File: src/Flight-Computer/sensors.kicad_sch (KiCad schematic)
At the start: 6 parts, among them U8 MPU-9250

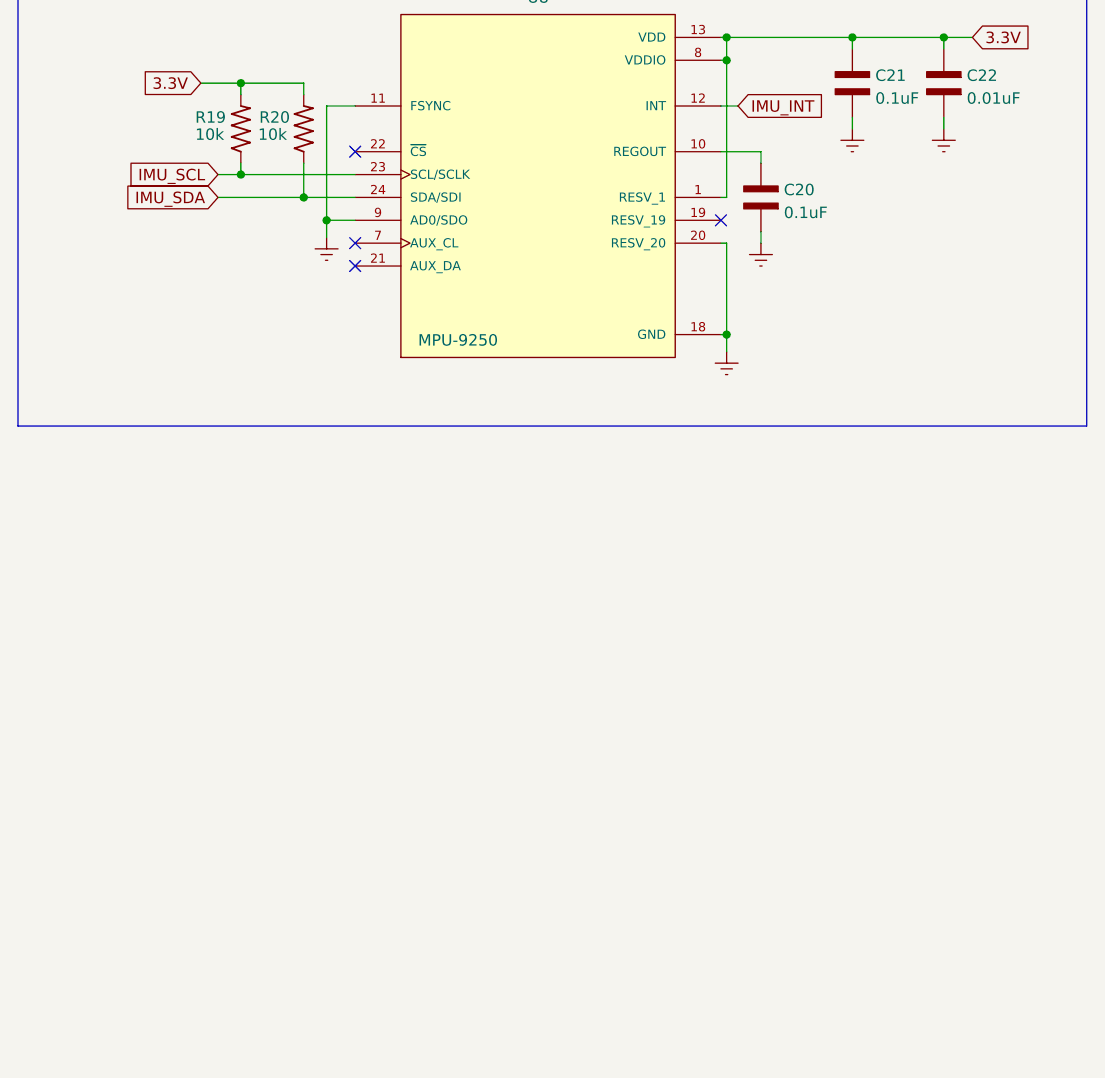
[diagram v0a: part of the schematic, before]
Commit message: added backup battery to lib files
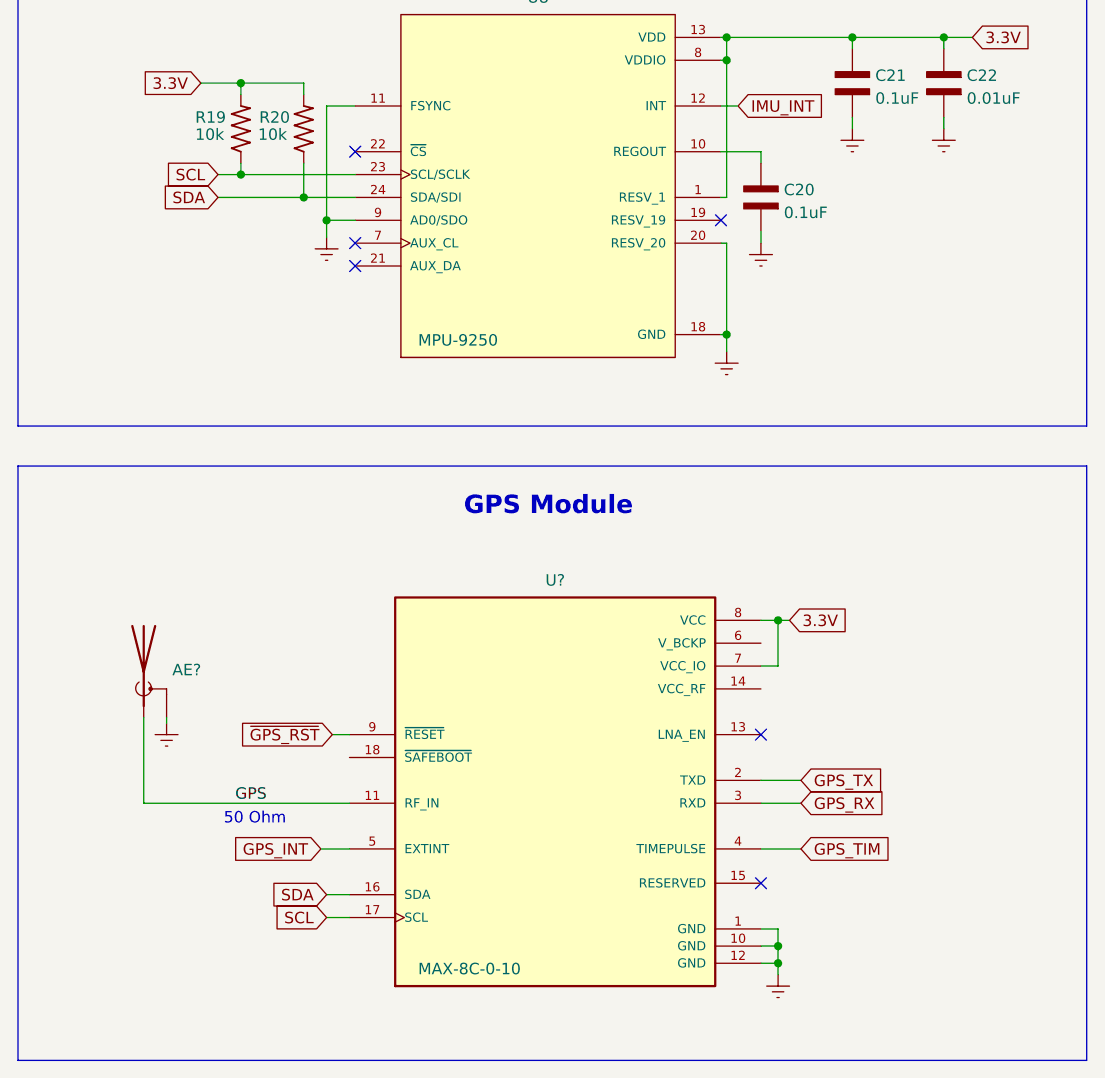
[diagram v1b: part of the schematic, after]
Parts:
- added AE?: 0734120110, symbol Flight-Computer:0734120110
- added U?: MAX-8C-0-10, XCVR_MAX-8C-0-10, symbol Flight-Computer:MAX-8C-0-10
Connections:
- net 3.3V: now also U?.7 (VCC_IO), U?.8 (VCC)
- net Earth: now also AE?.2 (Shield), U?.1 (GND), U?.10 (GND), U?.12 (GND)
- net IMU_SCL renamed SCL
- net SCL: now also U?.17 (SCL)
- net IMU_SDA renamed SDA
- net SDA: now also U?.16 (SDA)
- new net GPS: AE?.1 (A), U?.11 (RF_IN)
- new net GPS_INT: U?.5 (EXTINT)
- new net GPS_RX: U?.3 (RXD)
- new net GPS_TIM: U?.4 (TIMEPULSE)
- new net GPS_TX: U?.2 (TXD)
- new net ~{GPS_RST}: U?.9 (~{RESET})
- no-connect marks 4 -> 6
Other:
- note added: "50 Ohm"
- note added: "GPS Module"

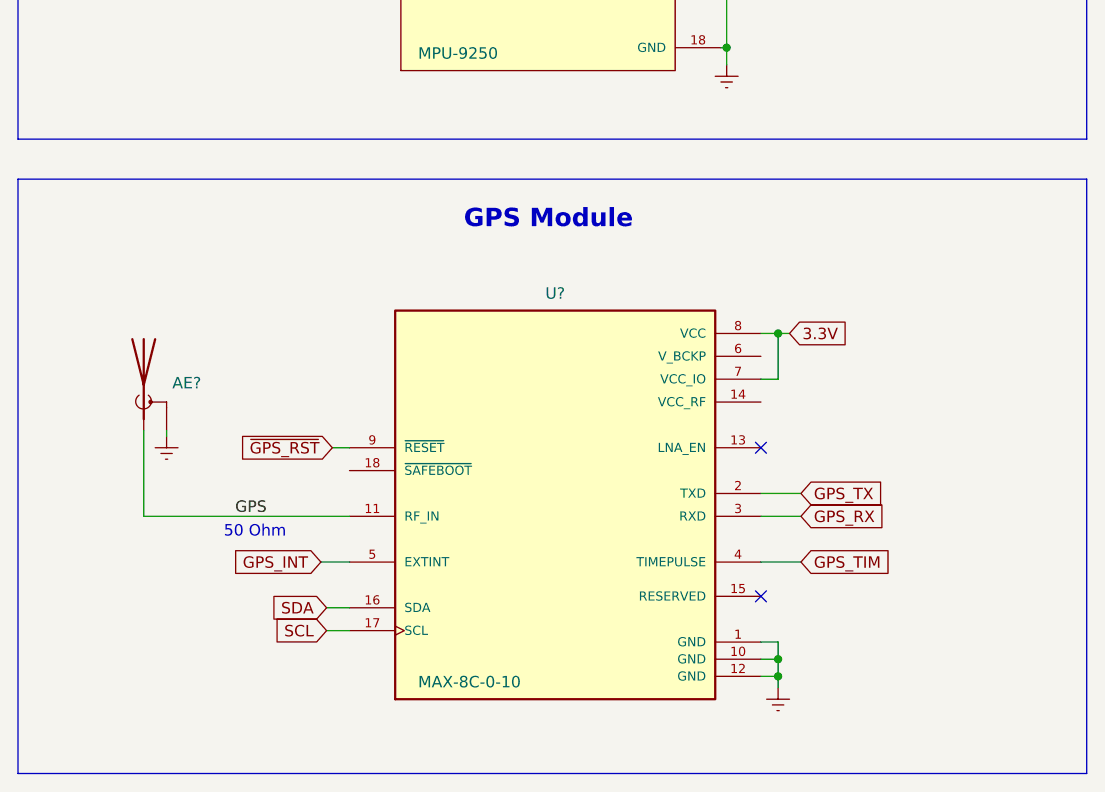
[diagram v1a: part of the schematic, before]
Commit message: implemented gps module for passive antenna design
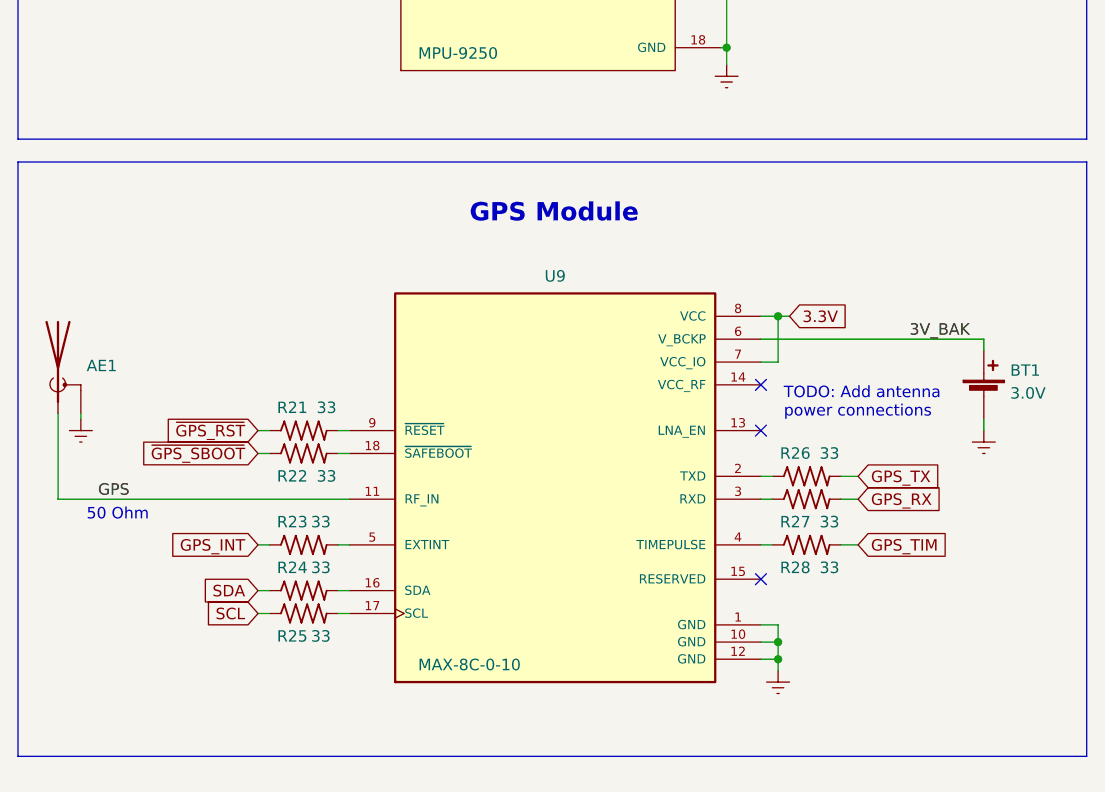
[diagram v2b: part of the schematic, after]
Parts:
- added BT1: MS614SE-FL28E, symbol Flight-Computer:MS614SE-FL28E
- added R21, R22, R23, R24, R25, R26, R27, R28: 33, symbol Flight-Computer:RES_0603
- gave numbers to parts that had none: 2
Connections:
- net Earth: now also BT1.2 (-)
- net GPS_INT: now also R23.1; no longer U9.5 (EXTINT)
- net GPS_RX: now also R27.2; no longer U9.3 (RXD)
- net GPS_TIM: now also R28.2; no longer U9.4 (TIMEPULSE)
- net GPS_TX: now also R26.2; no longer U9.2 (TXD)
- net SCL: now also R25.1; no longer U9.17 (SCL)
- net SDA: now also R24.1; no longer U9.16 (SDA)
- net ~{GPS_RST}: now also R21.1; no longer U9.9 (~{RESET})
- net at U9.18 (~{SAFEBOOT}): now also R22.2
- net 3V_BAK: now reaches U9.6 (V_BCKP)
- net 3V_BAK: now also BT1.1 (+)
- new net: R25.2, U9.17 (SCL)
- new net: R28.1, U9.4 (TIMEPULSE)
- new net: R23.2, U9.5 (EXTINT)
- new net: R24.2, U9.16 (SDA)
- new net: R26.1, U9.2 (TXD)
- new net: R27.1, U9.3 (RXD)
- new net: R21.2, U9.9 (~{RESET})
- new net ~{GPS_SBOOT}: R22.1
- no-connect marks 6 -> 7
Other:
- note added: "TODO: Add antenna power connections"
- moved on the sheet: AE1, U9

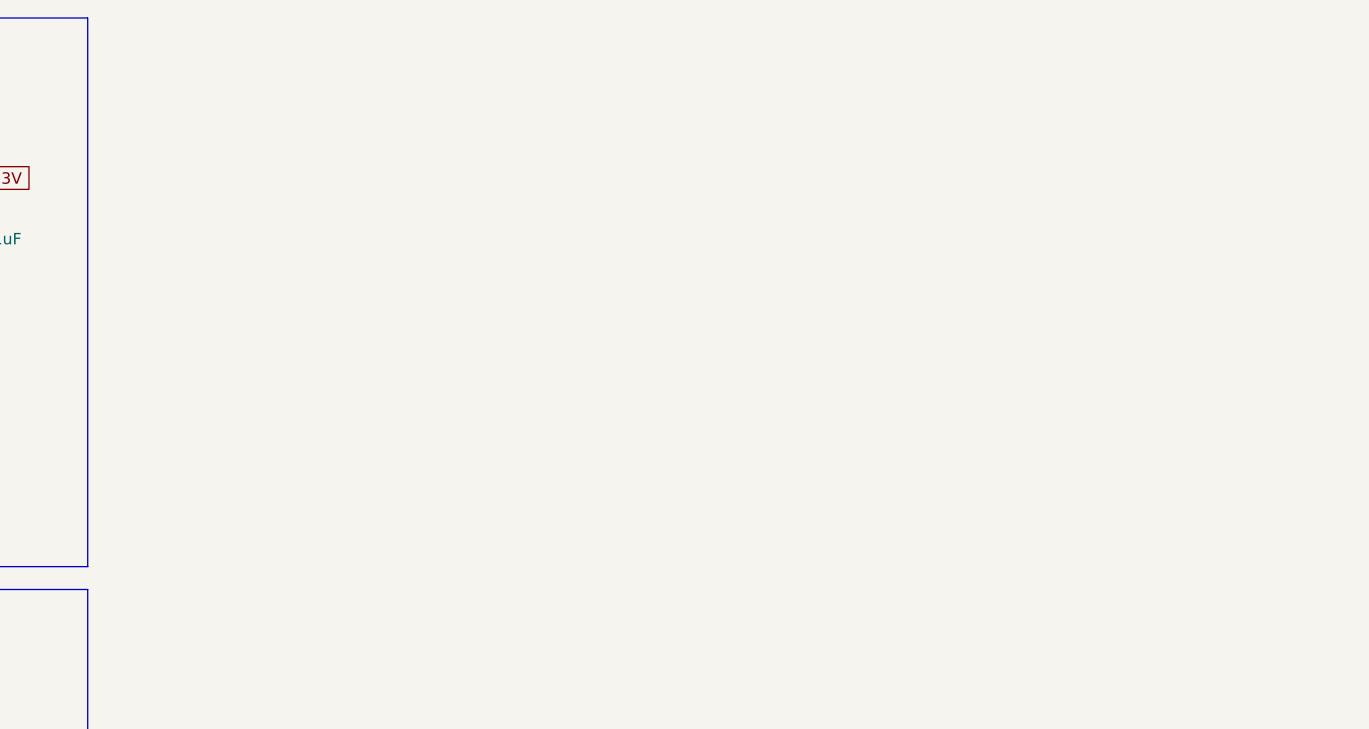
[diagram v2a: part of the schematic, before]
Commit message: implemented barometric pressure sensor in schematic
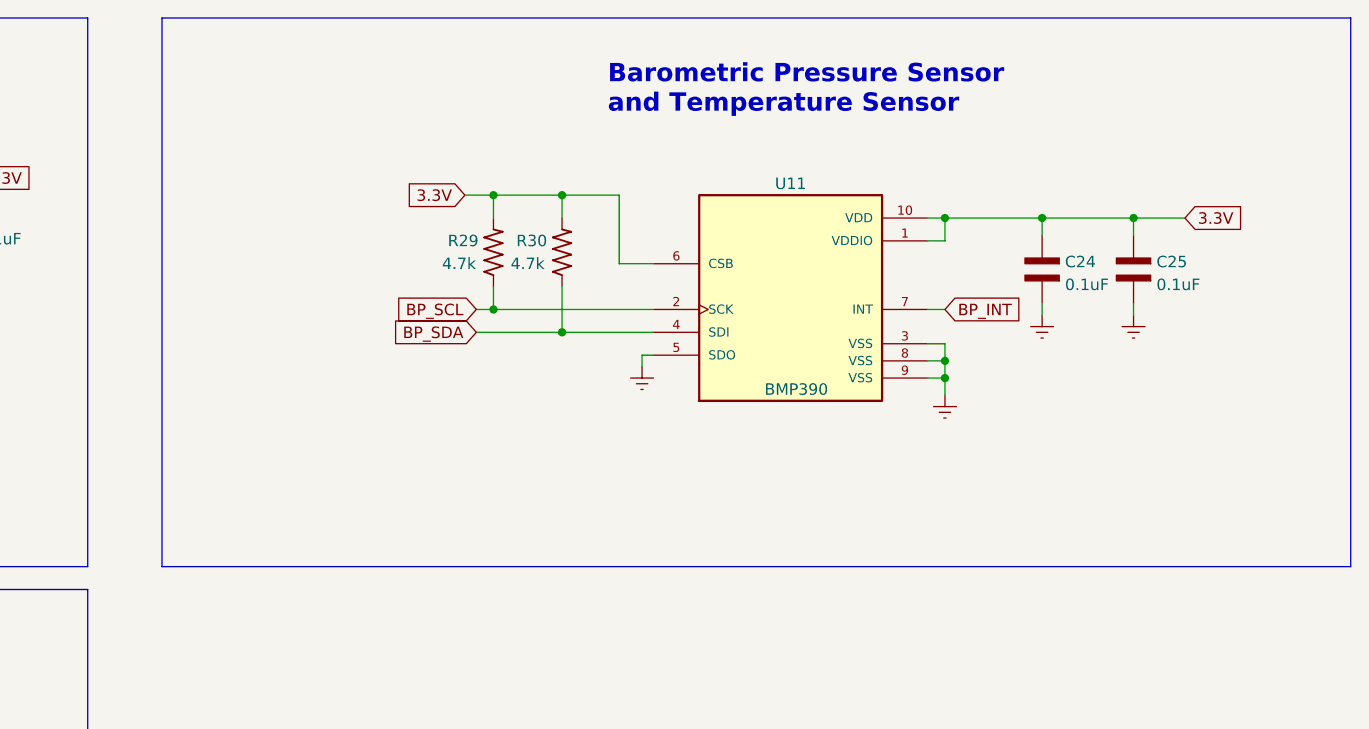
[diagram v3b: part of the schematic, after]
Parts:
- added C24, C25: 0.1uF, symbol Flight-Computer:CAP_0603
- added R29, R30: 4.7k, symbol Flight-Computer:RES_0603
- added U11: BMP390, XDCR_BMP390L, symbol Flight-Computer:BMP390
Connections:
- net 3.3V: now also C24.1, C25.1, R29.2, R30.2, U11.1 (VDDIO), U11.10 (VDD), U11.6 (CSB)
- net Earth: now also C24.2, C25.2, U11.3 (VSS), U11.5 (SDO), U11.8 (VSS), U11.9 (VSS)
- new net BP_INT: U11.7 (INT)
- new net BP_SCL: R29.1, U11.2 (SCK)
- new net BP_SDA: R30.1, U11.4 (SDI)
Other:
- note added: "Barometric Pressure Sensor and Temperature Sensor"

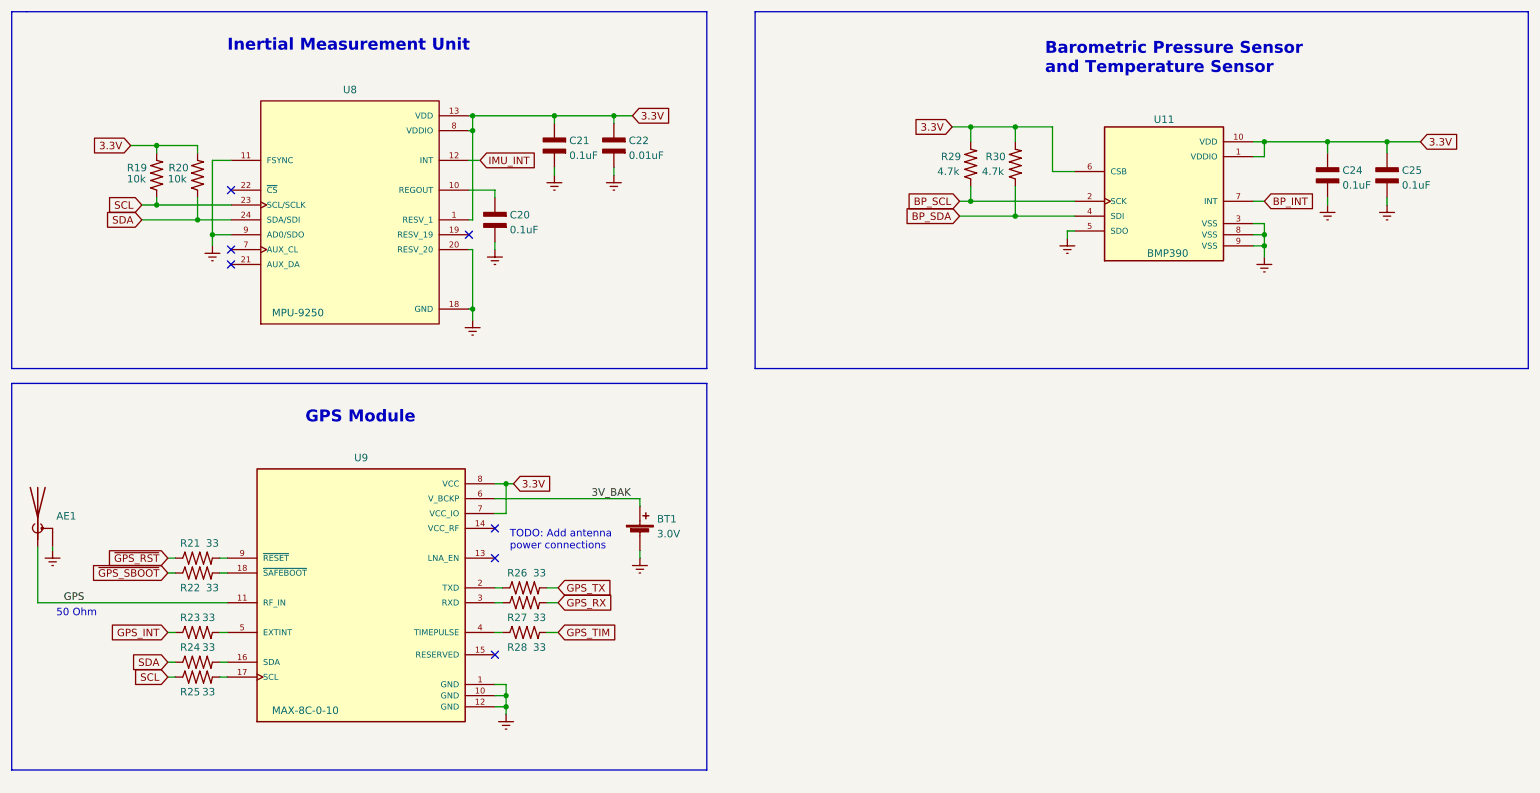
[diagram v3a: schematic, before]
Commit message: added zener diode to lib files
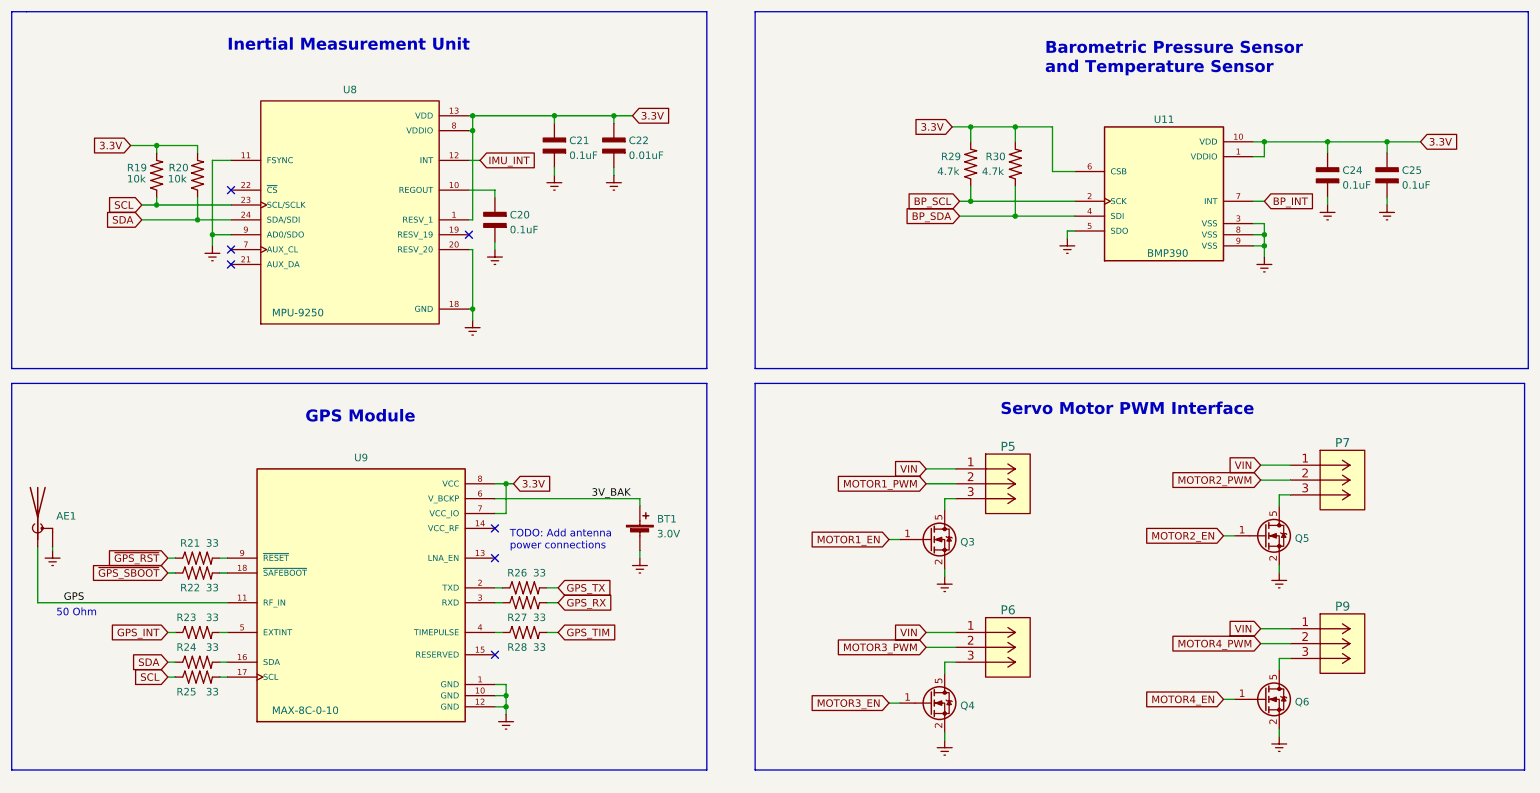
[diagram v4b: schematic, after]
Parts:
- added P5, P6, P7, P9: 440054-3, CONN_4840.2201_SCH, symbol Flight-Computer:440054-3
- added Q3, Q4, Q5, Q6: QS5U17TR, Package_TO_SOT_THT:TO-92_Inline, symbol Flight-Computer:QS5U17TR
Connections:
- net Earth: now also Q3.2 (S), Q4.2 (S), Q5.2 (S), Q6.2 (S)
- new net: P7.3, Q5.5 (D)
- new net: P5.3, Q3.5 (D)
- new net: P9.3, Q6.5 (D)
- new net: P6.3, Q4.5 (D)
- new net MOTOR1_EN: Q3.1 (G)
- new net MOTOR1_PWM: P5.2 (GND)
- new net MOTOR2_EN: Q5.1 (G)
- new net MOTOR2_PWM: P7.2 (GND)
- new net MOTOR3_EN: Q4.1 (G)
- new net MOTOR3_PWM: P6.2 (GND)
- new net MOTOR4_EN: Q6.1 (G)
- new net MOTOR4_PWM: P9.2 (GND)
- new net VIN: P5.1 (+12V), P6.1 (+12V), P7.1 (+12V), P9.1 (+12V)
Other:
- note added: "Servo Motor PWM Interface"
